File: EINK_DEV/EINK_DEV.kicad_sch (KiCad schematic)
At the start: 19 parts, among them J1 FPC, Q1 NMOS, U1 STM32WB55CEUx

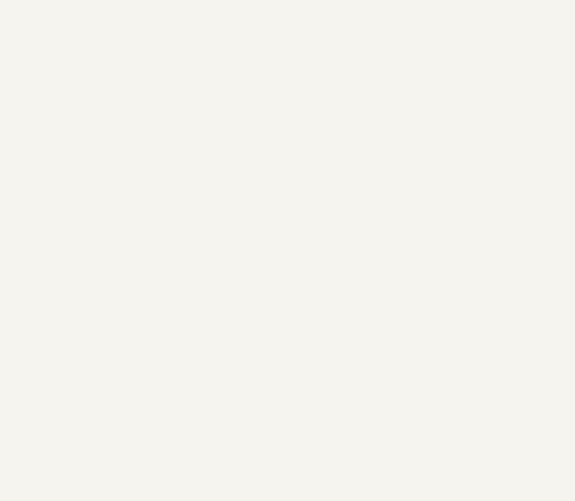
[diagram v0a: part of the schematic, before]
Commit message: Add micro-USB input
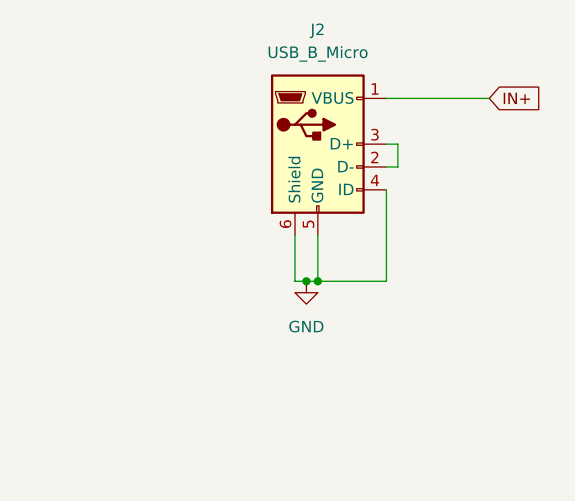
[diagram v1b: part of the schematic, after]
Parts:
- added J2: USB_B_Micro, symbol Connector:USB_B_Micro
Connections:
- net GND: now also J2.4 (ID), J2.5 (GND), J2.6 (Shield)
- new net: J2.2 (D-), J2.3 (D+)
- new net IN+: J2.1 (VBUS)

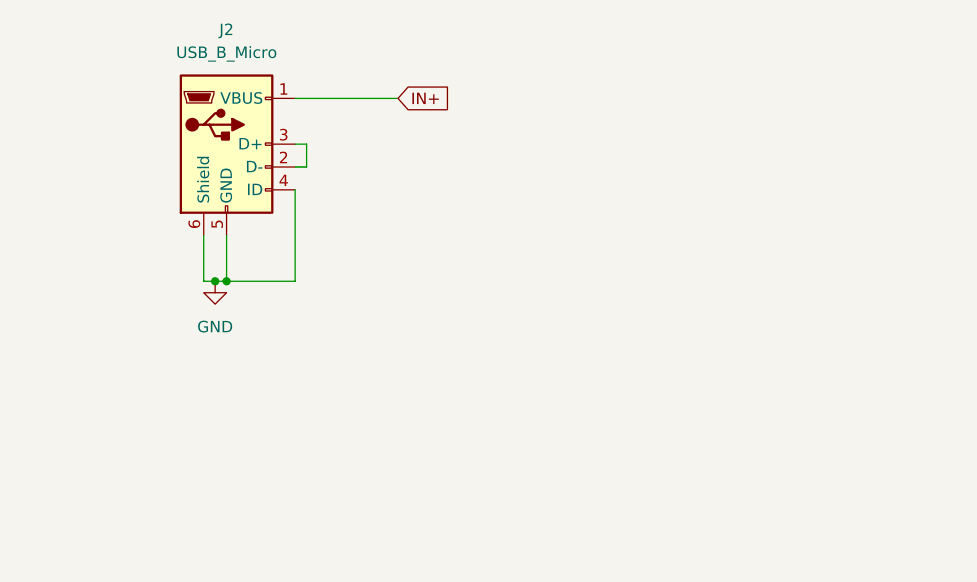
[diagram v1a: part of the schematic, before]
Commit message: Add D+ and D- flag
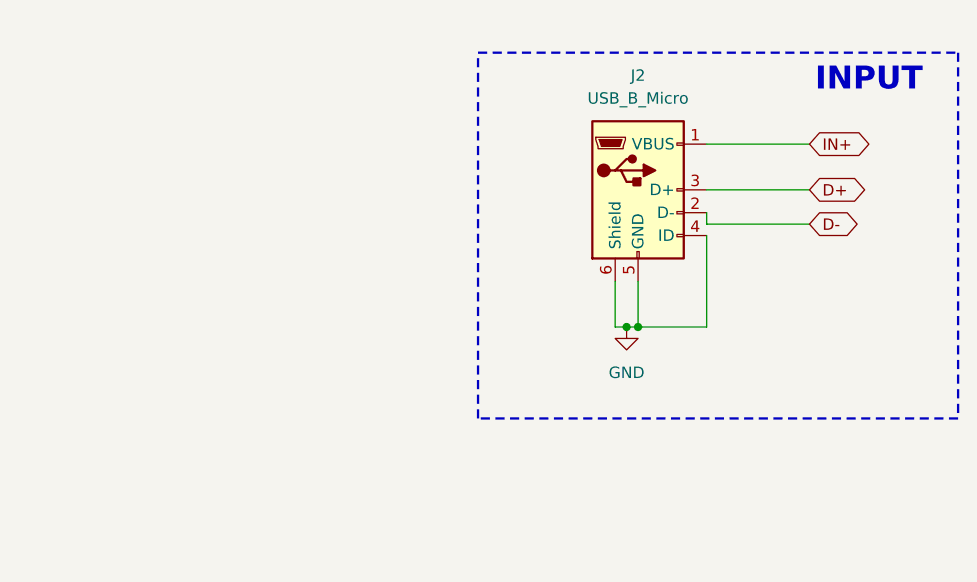
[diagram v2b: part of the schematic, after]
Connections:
- net D+: now reaches J2.3 (D+)
- net D+: no longer J2.2 (D-)
- new net D-: J2.2 (D-)
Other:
- note added: "INPUT"
- moved on the sheet: J2
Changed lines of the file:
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@@
+		)
+	)
+	(rectangle
+		(start 219.71 19.05)
+		(end 273.05 59.69)
+		(stroke
+			(width 0.254)
+			(type dash)
+		)
+		(fill
+			(type none)
+		)
+	)
+	(text "INPUT"
+		(exclude_from_sim no)
+		(at 263.144 22.098 0)
+		(effects
+			(font
+				(size 2.54 2.54)
+				(thickness 0.508)
+				(bold yes)
+			)
 		)
 	)
@@
 	)
 	(junction
-		(at 190.5 44.45)
+		(at 236.22 49.53)
 		(diameter 0)
 		(color 0 0 0 0)
@@
 	)
 	(junction
-		(at 191.77 44.45)
+		(at 237.49 49.53)
 		(diameter 0)
 		(color 0 0 0 0)
@@
 	(wire
 		(pts
-			(xy 199.39 31.75) (xy 200.66 31.75)
-		)
-		(stroke
-			(width 0)
-			(type default)
-		)
-	)
-	(wire
-		(pts
 			(xy 69.85 165.1) (xy 86.36 165.1)
 		)
@@
 	(wire
 		(pts
-			(xy 189.23 39.37) (xy 189.23 44.45)
+			(xy 234.95 44.45) (xy 234.95 49.53)
 		)
 		(stroke
@@
 	(wire
 		(pts
-			(xy 199.39 24.13) (xy 210.82 24.13)
+			(xy 245.11 29.21) (xy 256.54 29.21)
+		)
+		(stroke
+			(width 0)
+			(type default)
+		)
+	)
+	(wire
+		(pts
+			(xy 245.11 38.1) (xy 245.11 36.83)
 		)
 		(stroke
@@
 	(wire
 		(pts
-			(xy 191.77 44.45) (xy 199.39 44.45)
+			(xy 237.49 49.53) (xy 245.11 49.53)
 		)
 		(stroke
@@
 	(wire
 		(pts
-			(xy 189.23 44.45) (xy 190.5 44.45)
+			(xy 234.95 49.53) (xy 236.22 49.53)
 		)
 		(stroke
@@
 	(wire
 		(pts
-			(xy 199.39 34.29) (xy 199.39 44.45)
+			(xy 245.11 39.37) (xy 245.11 49.53)
 		)
 		(stroke
@@
 	(wire
 		(pts
+			(xy 245.11 34.29) (xy 256.54 34.29)
+		)
+		(stroke
+			(width 0)
+			(type default)
+		)
+	)
+	(wire
+		(pts
 			(xy 138.43 179.07) (xy 144.78 179.07)
 		)
@@
 	(wire
 		(pts
-			(xy 191.77 44.45) (xy 191.77 39.37)
-		)
-		(stroke
-			(width 0)
-			(type default)
-		)
-	)
-	(wire
-		(pts
-			(xy 199.39 29.21) (xy 200.66 29.21)
+			(xy 237.49 49.53) (xy 237.49 44.45)
 		)
 		(stroke
@@
 	(wire
 		(pts
-			(xy 190.5 44.45) (xy 191.77 44.45)
+			(xy 236.22 49.53) (xy 237.49 49.53)
 		)
 		(stroke
@@
 	(wire
 		(pts
+			(xy 256.54 38.1) (xy 245.11 38.1)
+		)
+		(stroke
+			(width 0)
+			(type default)
+		)
+	)
+	(wire
+		(pts
 			(xy 138.43 173.99) (xy 158.75 173.99)
 		)
@@
 		)
 	)
-	(wire
-		(pts
-			(xy 200.66 31.75) (xy 200.66 29.21)
-		)
-		(stroke
-			(width 0)
-			(type default)
-		)
-	)
 	(global_label "VGH"
 		(shape bidirectional)
@@
 		)
 	)
+	(global_label "D-"
+		(shape bidirectional)
+		(at 256.54 38.1 0)
+		(fields_autoplaced yes)
+		(effects
+			(font
+				(size 1.27 1.27)
+			)
+			(justify left)
+		)
+		(property "Intersheetrefs" "${INTERSHEET_REFS}"
+			(at 262.3676 38.1 0)
+			(effects
+				(font
+					(size 1.27 1.27)
+				)
+				(justify left)
+				(hide yes)
+			)
+		)
+	)
 	(global_label "CS#"
 		(shape bidirectional)
@@
 		)
 	)
+	(global_label "D+"
+		(shape bidirectional)
+		(at 256.54 34.29 0)
+		(fields_autoplaced yes)
+		(effects
+			(font
+				(size 1.27 1.27)
+			)
+			(justify left)
+		)
+		(property "Intersheetrefs" "${INTERSHEET_REFS}"
+			(at 262.3676 34.29 0)
+			(effects
+				(font
+					(size 1.27 1.27)
+				)
+				(justify left)
+				(hide yes)
+			)
+		)
+	)
 	(global_label "VGH"
 		(shape bidirectional)
@@
 	)
 	(global_label "IN+"
-		(shape input)
-		(at 210.82 24.13 0)
+		(shape bidirectional)
+		(at 256.54 29.21 0)
 		(fields_autoplaced yes)
 		(effects
@@
 		)
 		(property "Intersheetrefs" "${INTERSHEET_REFS}"
-			(at 217.3129 24.13 0)
+			(at 263.0329 29.21 0)
 			(effects
 				(font
@@
 	(symbol
 		(lib_id "Connector:USB_B_Micro")
-		(at 191.77 29.21 0)
+		(at 237.49 34.29 0)
 		(unit 1)
 		(exclude_from_sim no)
@@
 		(fields_autoplaced yes)
 		(property "Reference" "J2"
-			(at 191.77 16.51 0)
+			(at 237.49 21.59 0)
 			(effects
 				(font
@@
 		)
 		(property "Value" "USB_B_Micro"
-			(at 191.77 19.05 0)
+			(at 237.49 24.13 0)
 			(effects
 				(font
@@
 		)
 		(property "Footprint" ""
-			(at 195.58 30.48 0)
+			(at 241.3 35.56 0)
 			(effects
 				(font
@@
 		)
 		(property "Datasheet" "~"
-			(at 195.58 30.48 0)
+			(at 241.3 35.56 0)
 			(effects
 				(font
@@
 		)
 		(property "Description" "USB Micro Type B connector"
-			(at 191.77 29.21 0)
+			(at 237.49 34.29 0)
 			(effects
 				(font
@@
 	(symbol
 		(lib_id "power:GND")
-		(at 190.5 44.45 0)
+		(at 236.22 49.53 0)
 		(unit 1)
 		(exclude_from_sim no)
@@
 		(fields_autoplaced yes)
 		(property "Reference" "#PWR012"
-			(at 190.5 50.8 0)
+			(at 236.22 55.88 0)
 			(effects
 				(font
@@
 		)
 		(property "Value" "GND"
-			(at 190.5 49.53 0)
+			(at 236.22 54.61 0)
 			(effects
 				(font
@@
 		)
 		(property "Footprint" ""
-			(at 190.5 44.45 0)
+			(at 236.22 49.53 0)
 			(effects
 				(font
@@
 		)
 		(property "Datasheet" ""
-			(at 190.5 44.45 0)
+			(at 236.22 49.53 0)
 			(effects
 				(font
@@
 		)
 		(property "Description" "Power symbol creates a global label with name \"GND\" , ground"
-			(at 190.5 44.45 0)
-			(effects
-				(font
+			(at 236.22 49.53 0)
+			(effects
+				(font

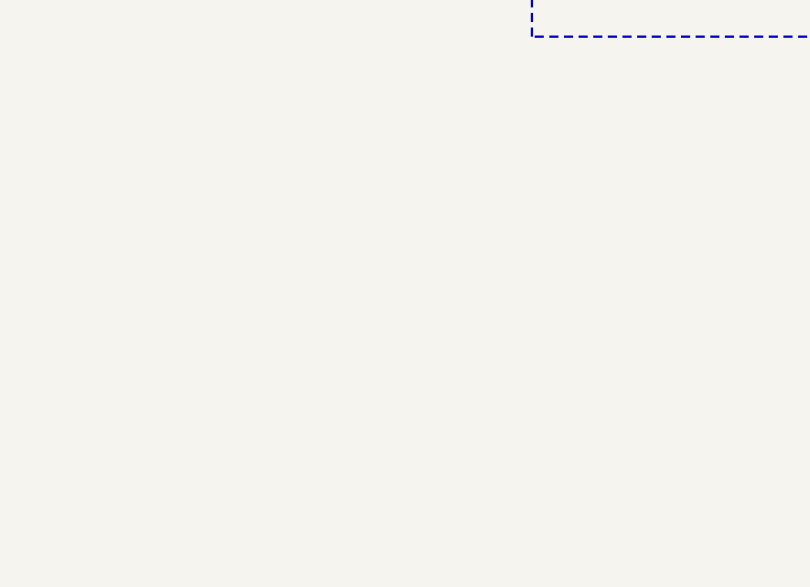
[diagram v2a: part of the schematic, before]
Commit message: Add TP4056 module
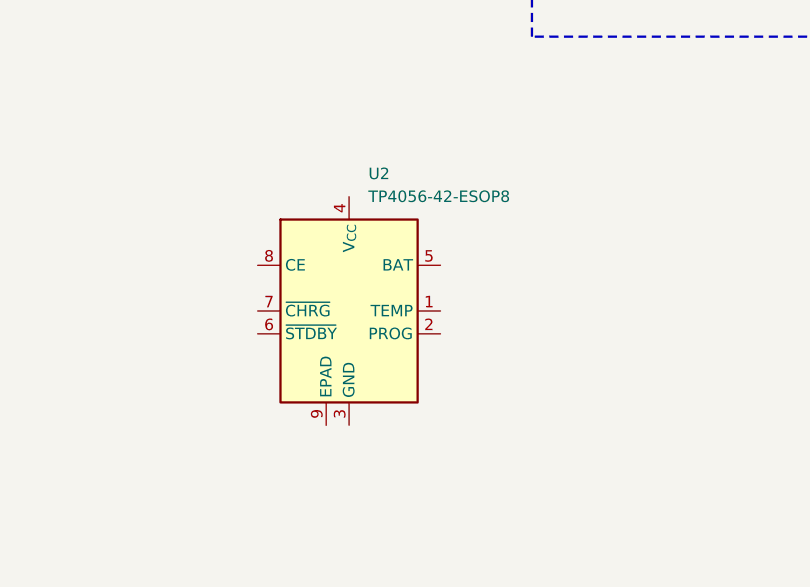
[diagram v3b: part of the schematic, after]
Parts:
- added U2: TP4056-42-ESOP8, Package_SO:SOIC-8-1EP_3.9x4.9mm_P1.27mm_EP2.41x3.3mm_ThermalVias, symbol Battery_Management:TP4056-42-ESOP8
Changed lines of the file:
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@@
+		)
+	)
+	(symbol
+		(lib_id "Battery_Management:TP4056-42-ESOP8")
+		(at 199.39 90.17 0)
+		(unit 1)
+		(exclude_from_sim no)
+		(in_bom yes)
+		(on_board yes)
+		(dnp no)
+		(fields_autoplaced yes)
+		(property "Reference" "U2"
+			(at 201.5333 74.93 0)
+			(effects
+				(font
+					(size 1.27 1.27)
+				)
+				(justify left)
+			)
+		)
+		(property "Value" "TP4056-42-ESOP8"
+			(at 201.5333 77.47 0)
+			(effects
+				(font
+					(size 1.27 1.27)
+				)
+				(justify left)
+			)
+		)
+		(property "Footprint" "Package_SO:SOIC-8-1EP_3.9x4.9mm_P1.27mm_EP2.41x3.3mm_ThermalVias"
+			(at 199.898 113.03 0)
+			(effects
+				(font
+					(size 1.27 1.27)
+				)
+				(hide yes)
+			)
+		)
+		(property "Datasheet" "https://www.lcsc.com/datasheet/lcsc_datasheet_2410121619_TOPPOWER-Nanjing-Extension-Microelectronics-TP4056-42-ESOP8_C16581.pdf"
+			(at 199.39 115.57 0)
+			(effects
+				(font
+					(size 1.27 1.27)
+				)
+				(hide yes)
+			)
+		)
+		(property "Description" "1A Standalone Linear Li-ion/LiPo single-cell battery charger, 4.2V ±1% charge voltage, VCC = 4.0..8.0V, SOIC-8 (SOP-8)"
+			(at 199.898 110.49 0)
+			(effects
+				(font
+					(size 1.27 1.27)
+				)
+				(hide yes)
+			)
+		)
+		(pin "1"
+		)
+		(pin "4"
+		)
+		(pin "6"
+		)
+		(pin "2"
+		)
+		(pin "7"
+		)
+		(pin "9"
+		)
+		(pin "8"
+		)
+		(pin "3"
+		)
+		(pin "5"
+		)
+		(instances
+			(project ""
+				(path "/21ffd272-94a2-4b6a-9954-5d1217824b1f"
+					(reference "U2")
+					(unit 1)
+				)
+			)
 		)
 	)

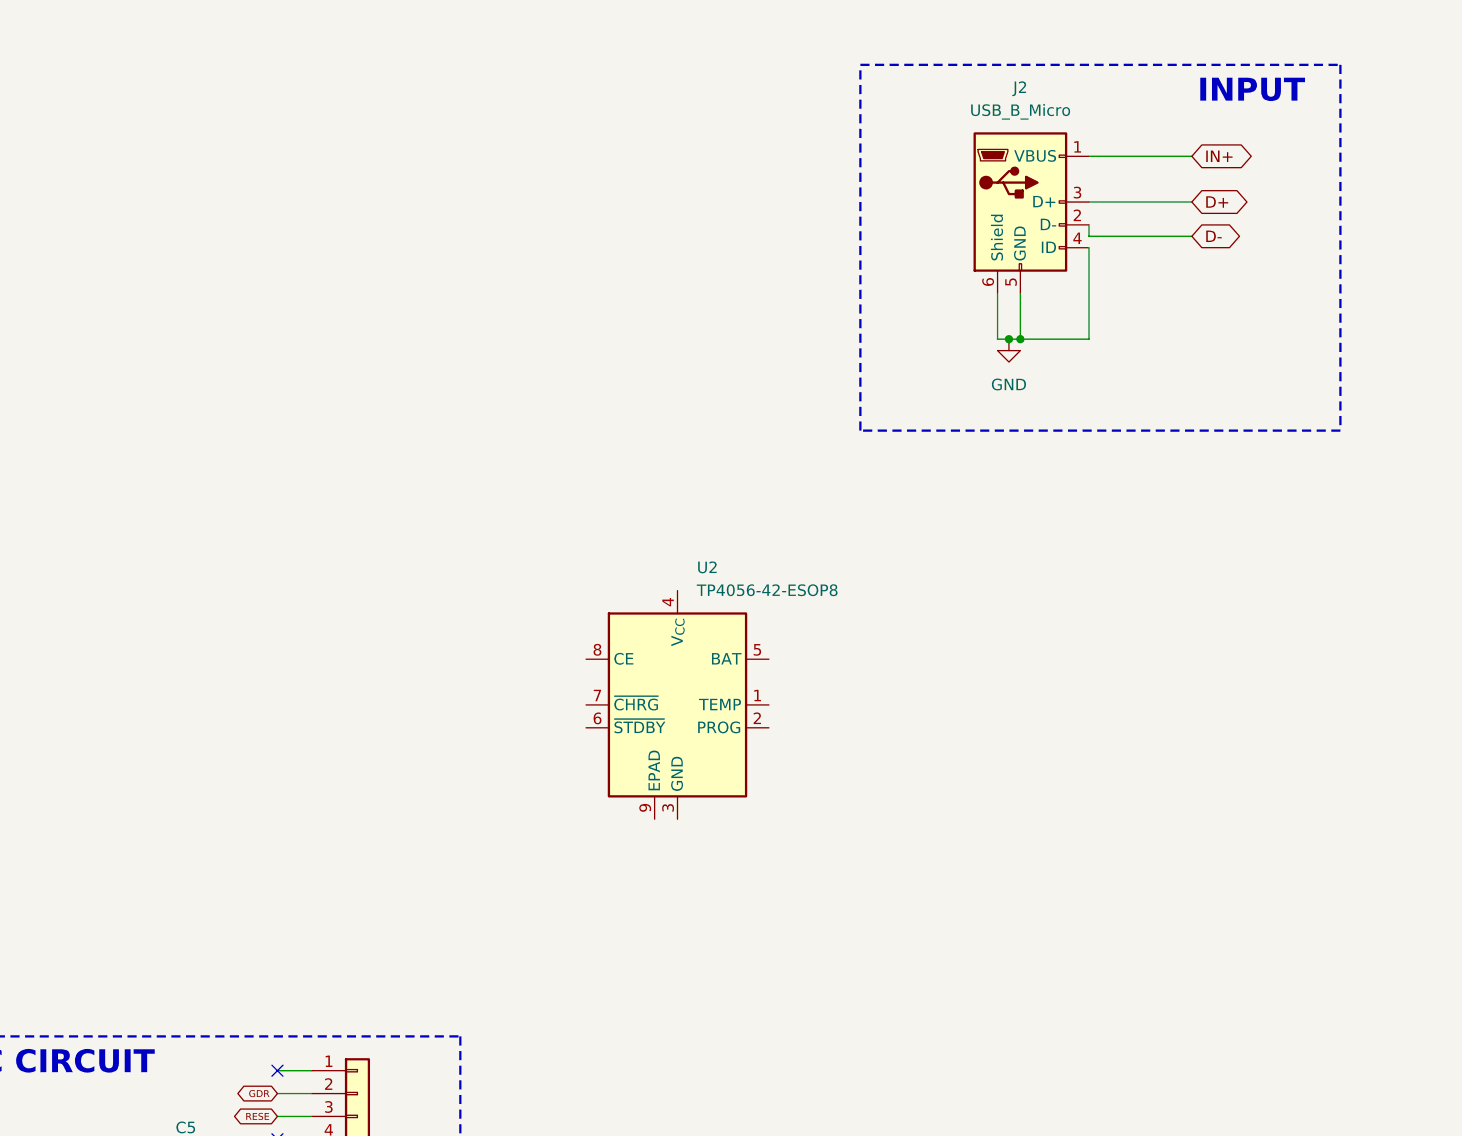
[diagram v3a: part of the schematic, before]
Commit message: Add charging module
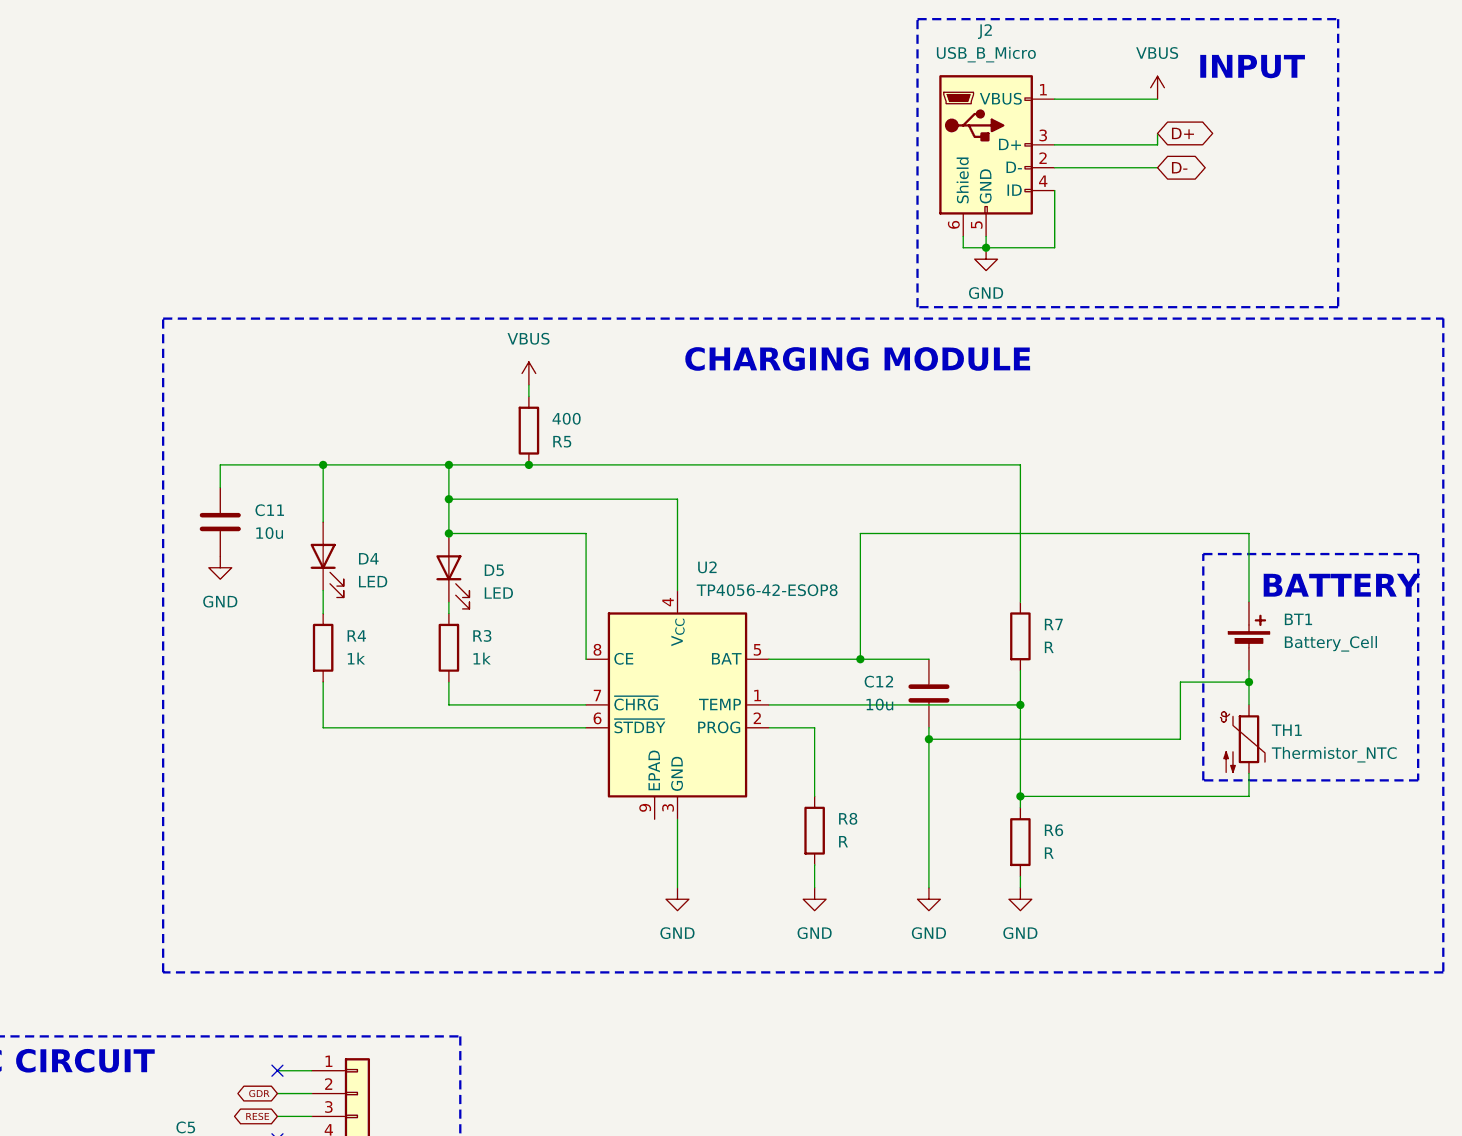
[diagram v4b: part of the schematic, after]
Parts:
- added BT1: Battery_Cell, symbol Device:Battery_Cell
- added C11, C12: 10u, symbol Device:C
- added D4, D5: LED, symbol Device:LED
- added R3, R4: 1k, symbol Device:R
- added R5: 400, symbol Device:R
- added R6, R7, R8: R, symbol Device:R
- added TH1: Thermistor_NTC, symbol Device:Thermistor_NTC
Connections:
- net GND: now also U2.3 (GND), BT1.2 (-), C11.2, C12.1, R6.2, R8.2, TH1.1
- net at U2.1 (TEMP): now also R6.1, R7.2, TH1.2
- net at U2.2 (PROG): now also R8.1
- net at U2.4 (V_{CC}): now also U2.8 (CE), C11.1, D4.2 (A), D5.2 (A), R5.1, R7.1
- net at U2.5 (BAT): now also BT1.1 (+), C12.2
- net at U2.6 (~{STDBY}): now also R4.2
- net at U2.7 (~{CHRG}): now also R3.1
- net IN+ renamed VBUS
- net VBUS: now also R5.2
- new net: D5.1 (K), R3.2
- new net: D4.1 (K), R4.1
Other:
- note added: "BATTERY"
- note added: "CHARGING MODULE"
- moved on the sheet: J2
